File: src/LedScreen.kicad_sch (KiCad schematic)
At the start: 38 parts

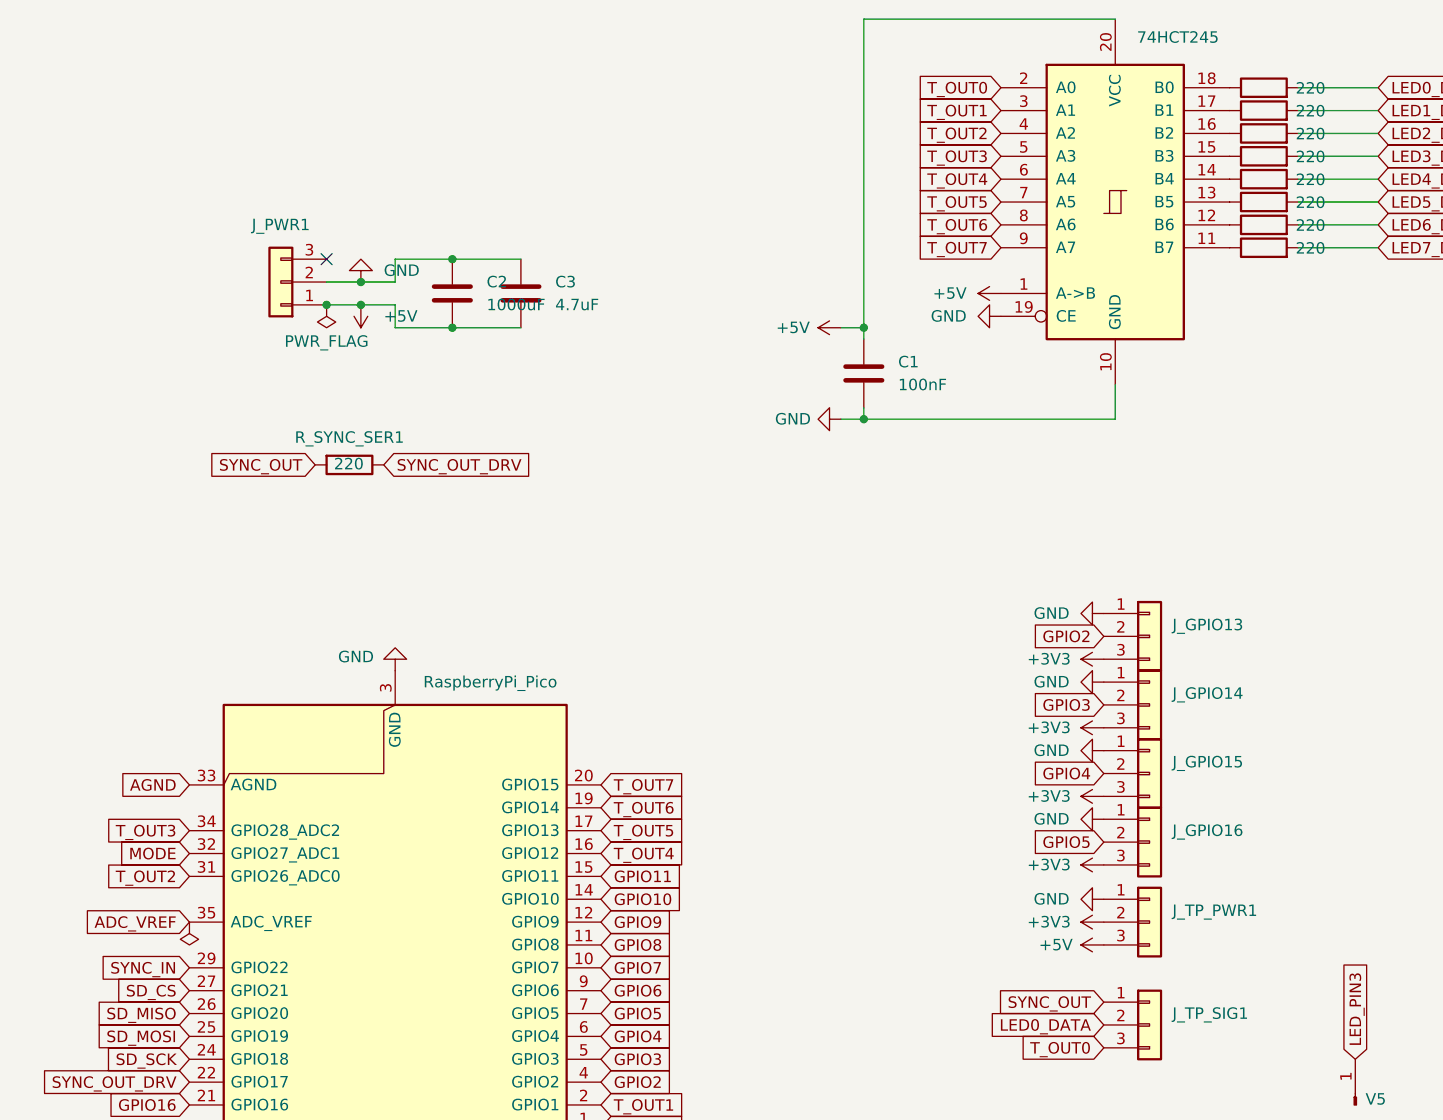
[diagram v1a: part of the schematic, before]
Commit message: added Bom+Journal
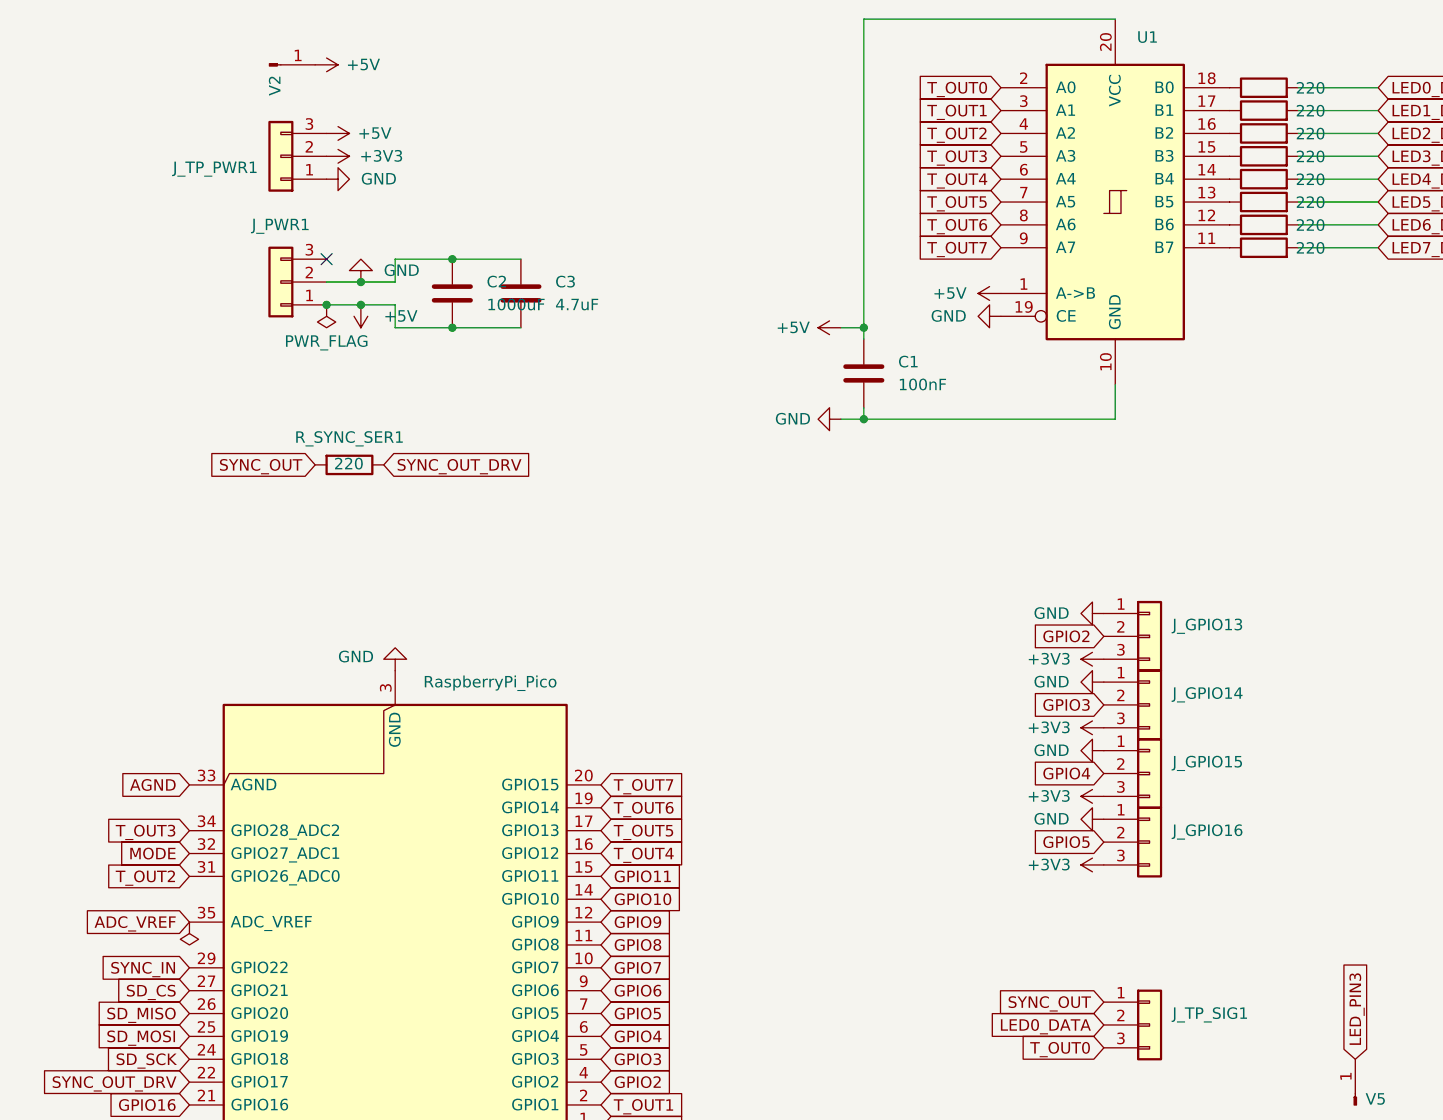
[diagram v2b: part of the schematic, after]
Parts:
- added V2: Conn_01x01_Pin, Connector_PinHeader_2.54mm:PinHeader_1x01_P2.54mm_Vertical, symbol Connector:Conn_01x01_Pin
- renumbered SD_READER1 to J1, 74HCT245 to U1
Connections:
- net +5V: now also V2.1 (Pin_1)
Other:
- moved on the sheet: J_TP_PWR1
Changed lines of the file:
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@@
 	(symbol
 		(lib_id "power:+3V3")
-		(at 132.08 132.08 90)
+		(at 45.72 46.99 270)
 		(unit 1)
 		(exclude_from_sim no)
@@
 		(dnp no)
 		(property "Reference" "#PWR019"
-			(at 135.89 132.08 0)
+			(at 41.91 46.99 0)
 			(effects
 				(font
@@
 		)
 		(property "Value" "+3V3"
-			(at 125.984 132.08 90)
+			(at 51.816 46.99 90)
 			(effects
 				(font
@@
 		)
 		(property "Footprint" ""
-			(at 132.08 132.08 0)
+			(at 45.72 46.99 0)
 			(effects
 				(font
@@
 		)
 		(property "Datasheet" ""
-			(at 132.08 132.08 0)
+			(at 45.72 46.99 0)
 			(effects
 				(font
@@
 		)
 		(property "Description" "Power symbol creates a global label with name \"+3V3\""
-			(at 132.08 132.08 0)
+			(at 45.72 46.99 0)
 			(effects
 				(font
@@
 	)
 	(symbol
+		(lib_id "Connector:Conn_01x01_Pin")
+		(at 39.37 36.83 0)
+		(unit 1)
+		(exclude_from_sim no)
+		(in_bom yes)
+		(on_board yes)
+		(dnp no)
+		(property "Reference" "V2"
+			(at 40.005 39.116 90)
+			(effects
+				(font
+					(size 1.27 1.27)
+				)
+			)
+		)
+		(property "Value" "Conn_01x01_Pin"
+			(at 37.465 37.084 90)
+			(effects
+				(font
+					(size 1.27 1.27)
+				)
+				(hide yes)
+			)
+		)
+		(property "Footprint" "Connector_PinHeader_2.54mm:PinHeader_1x01_P2.54mm_Vertical"
+			(at 38.608 35.052 0)
+			(effects
+				(font
+					(size 1.27 1.27)
+				)
+				(hide yes)
+			)
+		)
+		(property "Datasheet" "~"
+			(at 39.37 36.83 0)
+			(effects
+				(font
+					(size 1.27 1.27)
+				)
+				(hide yes)
+			)
+		)
+		(property "Description" "Generic connector, single row, 01x01, script generated"
+			(at 39.37 36.83 0)
+			(effects
+				(font
+					(size 1.27 1.27)
+				)
+				(hide yes)
+			)
+		)
+		(pin "1"
+		)
+		(instances
+			(project "LedScreen"
+				(path "/6393ae6b-20d3-4709-8a4f-a83a956b3492"
+					(reference "V2")
+					(unit 1)
+				)
+			)
+		)
+	)
+	(symbol
 		(lib_id "Connector_Generic:Conn_01x02")
 		(at 151.13 175.26 0)
@@
 		(on_board yes)
 		(dnp no)
-		(property "Reference" "74HCT245"
+		(property "Reference" "U1"
 			(at 135.7473 33.782 0)
 			(effects
@@
 			(project ""
 				(path "/6393ae6b-20d3-4709-8a4f-a83a956b3492"
-					(reference "74HCT245")
+					(reference "U1")
 					(unit 1)
 				)
@@
 	(symbol
 		(lib_id "power:+5V")
+		(at 44.45 36.83 270)
+		(unit 1)
+		(exclude_from_sim no)
+		(in_bom yes)
+		(on_board yes)
+		(dnp no)
+		(property "Reference" "#PWR046"
+			(at 40.64 36.83 0)
+			(effects
+				(font
+					(size 1.27 1.27)
+				)
+				(hide yes)
+			)
+		)
+		(property "Value" "+5V"
+			(at 49.784 36.83 90)
+			(effects
+				(font
+					(size 1.27 1.27)
+				)
+			)
+		)
+		(property "Footprint" ""
+			(at 44.45 36.83 0)
+			(effects
+				(font
+					(size 1.27 1.27)
+				)
+				(hide yes)
+			)
+		)
+		(property "Datasheet" ""
+			(at 44.45 36.83 0)
+			(effects
+				(font
+					(size 1.27 1.27)
+				)
+				(hide yes)
+			)
+		)
+		(property "Description" "Power symbol creates a global label with name \"+5V\""
+			(at 44.45 36.83 0)
+			(effects
+				(font
+					(size 1.27 1.27)
+				)
+				(hide yes)
+			)
+		)
+		(pin "1"
+		)
+		(instances
+			(project "LedScreen"
+				(path "/6393ae6b-20d3-4709-8a4f-a83a956b3492"
+					(reference "#PWR046")
+					(unit 1)
+				)
+			)
+		)
+	)
+	(symbol
+		(lib_id "power:+5V")
 		(at 182.88 111.76 90)
 		(unit 1)
@@
 	(symbol
 		(lib_id "Connector_Generic:Conn_01x03")
-		(at 137.16 132.08 0)
+		(at 40.64 46.99 180)
 		(unit 1)
 		(exclude_from_sim no)
@@
 		(fields_autoplaced yes)
 		(property "Reference" "J_TP_PWR1"
-			(at 139.7 130.8099 0)
+			(at 38.1 48.2601 0)
 			(effects
 				(font
@@
 		)
 		(property "Value" "TP_PWR"
-			(at 139.7 133.3499 0)
+			(at 38.1 45.7201 0)
 			(effects
 				(font
@@
 		)
 		(property "Footprint" "Connector_PinHeader_2.54mm:PinHeader_1x03_P2.54mm_Vertical"
-			(at 137.16 132.08 0)
+			(at 40.64 46.99 0)
 			(effects
 				(font
@@
 		)
 		(property "Datasheet" "~"
-			(at 137.16 132.08 0)
+			(at 40.64 46.99 0)
 			(effects
 				(font
@@
 		)
 		(property "Description" "Generic connector, single row, 01x03, script generated (kicad-library-utils/schlib/autogen/connector/)"
-			(at 137.16 132.08 0)
+			(at 40.64 46.99 0)
 			(effects
 				(font
@@
 	(symbol
 		(lib_id "power:+5V")
-		(at 132.08 134.62 90)
+		(at 45.72 44.45 270)
 		(unit 1)
 		(exclude_from_sim no)
@@
 		(dnp no)
 		(property "Reference" "#PWR030"
-			(at 135.89 134.62 0)
+			(at 41.91 44.45 0)
 			(effects
 				(font
@@
 		)
 		(property "Value" "+5V"
-			(at 126.746 134.62 90)
+			(at 51.054 44.45 90)
 			(effects
 				(font
@@
 		)
 		(property "Footprint" ""
-			(at 132.08 134.62 0)
+			(at 45.72 44.45 0)
 			(effects
 				(font
@@
 		)
 		(property "Datasheet" ""
-			(at 132.08 134.62 0)
+			(at 45.72 44.45 0)
 			(effects
 				(font
@@
 		)
 		(property "Description" "Power symbol creates a global label with name \"+5V\""
-			(at 132.08 134.62 0)
+			(at 45.72 44.45 0)
 			(effects
 				(font
@@
 	(symbol
 		(lib_id "power:GND")
-		(at 132.08 129.54 270)
+		(at 45.72 49.53 90)
 		(unit 1)
 		(exclude_from_sim no)
@@
 		(fields_autoplaced yes)
 		(property "Reference" "#PWR032"
-			(at 125.73 129.54 0)
+			(at 52.07 49.53 0)
 			(effects
 				(font
@@
 		)
 		(property "Value" "GND"
-			(at 128.27 129.5399 90)
+			(at 49.53 49.5301 90)
 			(effects
 				(font
@@
 		)
 		(property "Footprint" ""
-			(at 132.08 129.54 0)
+			(at 45.72 49.53 0)
 			(effects
 				(font
@@
 		)
 		(property "Datasheet" ""
-			(at 132.08 129.54 0)
+			(at 45.72 49.53 0)
 			(effects
 				(font
@@
 		)
 		(property "Description" "Power symbol creates a global label with name \"GND\" , ground"
-			(at 132.08 129.54 0)
+			(at 45.72 49.53 0)
 			(effects
 				(font
@@
 		(on_board yes)
 		(dnp no)
-		(property "Reference" "SD_READER1"
+		(property "Reference" "J1"
 			(at 242.951 28.194 0)
 			(effects
@@
 			(project ""
 				(path "/6393ae6b-20d3-4709-8a4f-a83a956b3492"
-					(reference "SD_READER1")
+					(reference "J1")
 					(unit 1)
 				)

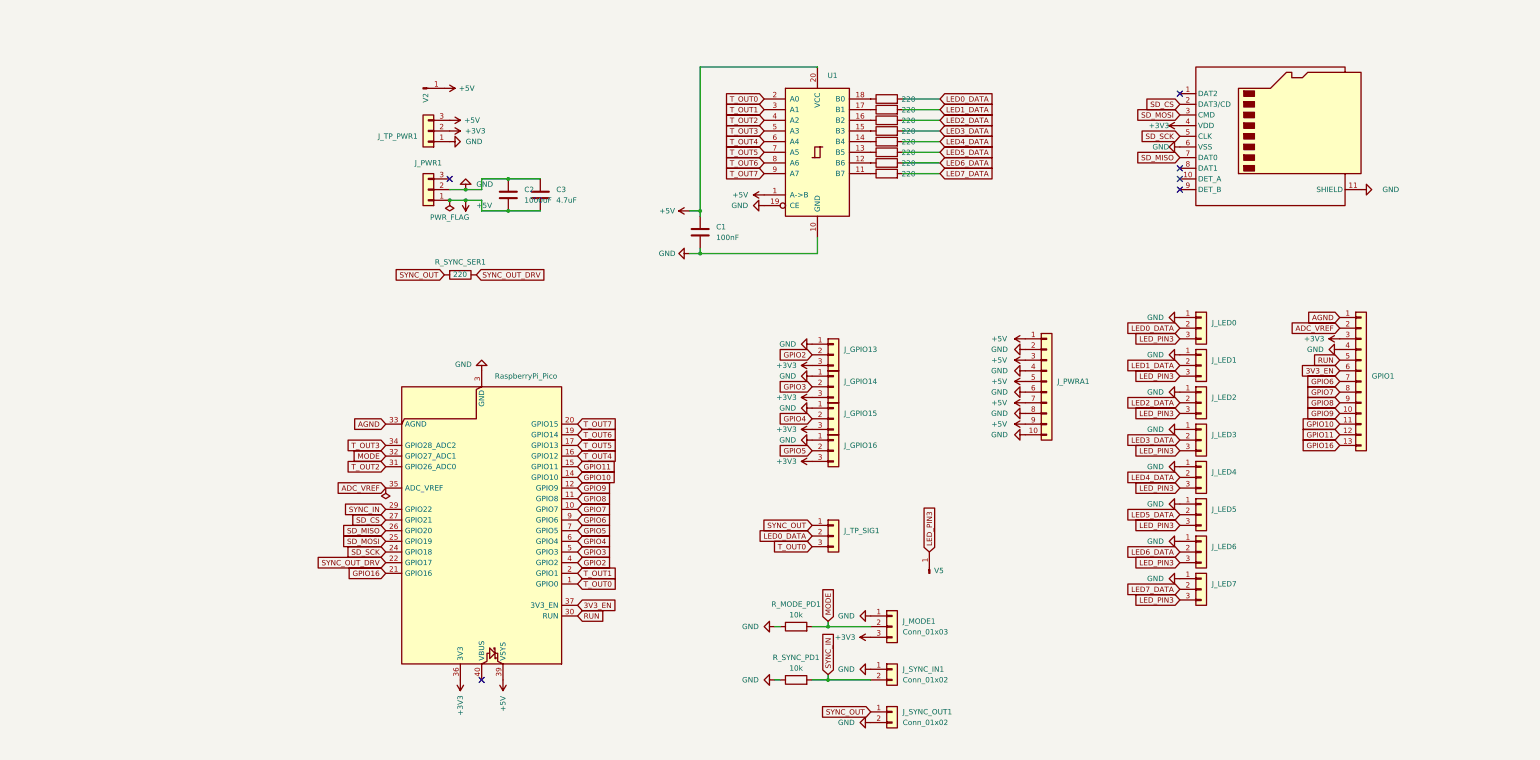
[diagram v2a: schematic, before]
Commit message: updated power injection wireing
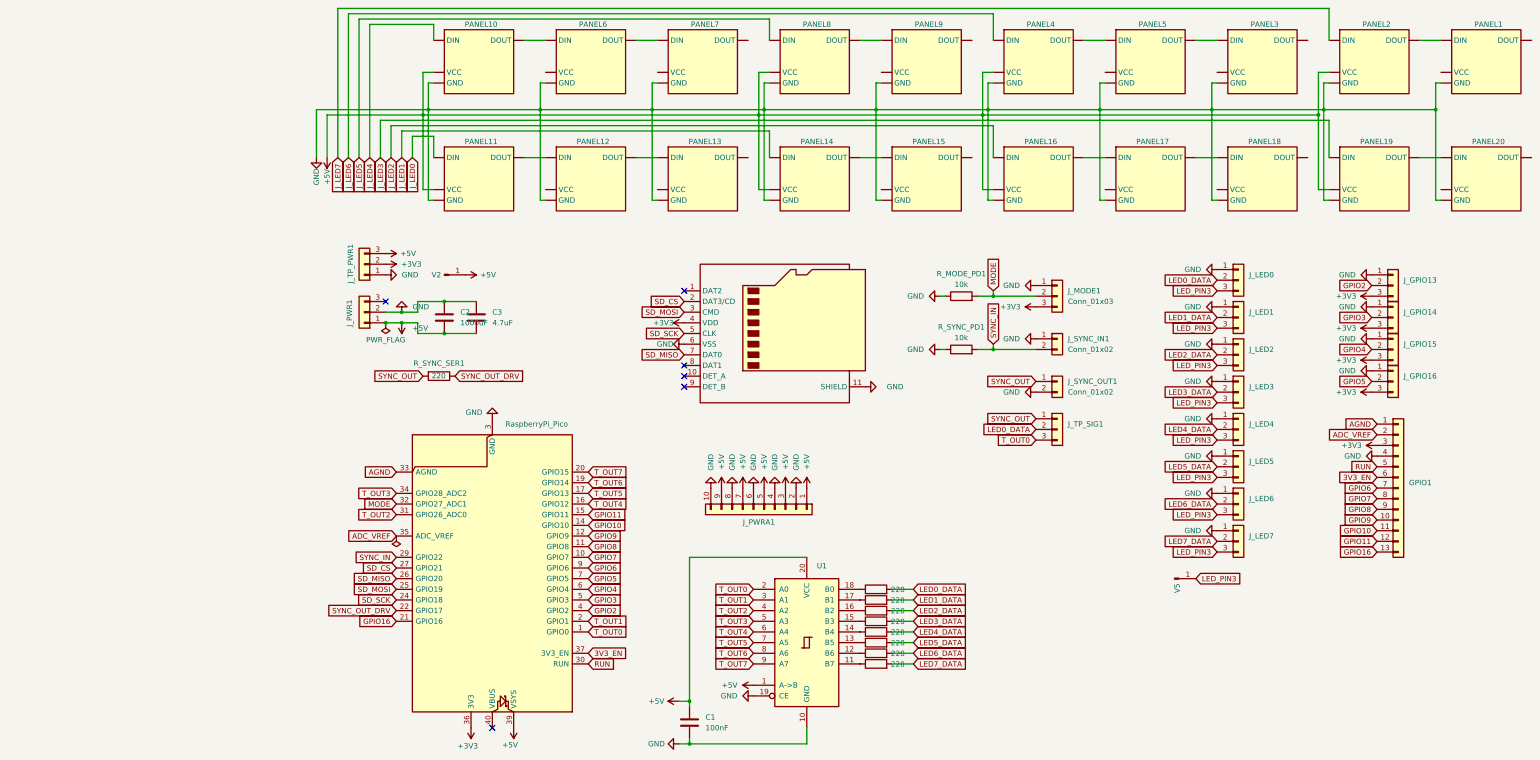
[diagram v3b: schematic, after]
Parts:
- added PANEL1, PANEL10, PANEL11, PANEL12, PANEL13, PANEL14, PANEL15, PANEL16, PANEL17, PANEL18, PANEL19, PANEL2, PANEL20, PANEL3, PANEL4, PANEL5, PANEL6, PANEL7, PANEL8, PANEL9: ~, symbol ledpanels:LED_PANEL_16x16
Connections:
- net +5V: now also PANEL10. (DOUT), PANEL11. (DOUT), PANEL14. (DOUT), PANEL16. (DOUT), PANEL19. (DOUT), PANEL2. (DOUT), PANEL4. (DOUT), PANEL8. (DOUT)
- net GND: now also PANEL1. (DOUT), PANEL10. (DOUT), PANEL11. (DOUT), PANEL12. (DOUT), PANEL13. (DOUT), PANEL14. (DOUT), PANEL15. (DOUT), PANEL16. (DOUT), PANEL17. (DOUT), PANEL18. (DOUT), PANEL19. (DOUT), PANEL2. (DOUT), PANEL20. (DOUT), PANEL3. (DOUT), PANEL4. (DOUT), PANEL5. (DOUT), PANEL6. (DOUT), PANEL7. (DOUT), PANEL8. (DOUT), PANEL9. (DOUT)
- new net: PANEL8. (DOUT), PANEL9. (DOUT)
- new net: PANEL4. (DOUT), PANEL5. (DOUT)
- new net: PANEL1. (DOUT), PANEL2. (DOUT)
- new net: PANEL19. (DOUT), PANEL20. (DOUT)
- new net: PANEL6. (DOUT), PANEL7. (DOUT)
- new net: PANEL16. (DOUT), PANEL17. (DOUT)
- new net: PANEL12. (DOUT), PANEL13. (DOUT)
- new net: PANEL3. (DOUT), PANEL5. (DOUT)
- new net: PANEL10. (DOUT), PANEL6. (DOUT)
- new net: PANEL17. (DOUT), PANEL18. (DOUT)
- new net: PANEL14. (DOUT), PANEL15. (DOUT)
- new net: PANEL11. (DOUT), PANEL12. (DOUT)
- new net J_LED0: PANEL11. (DOUT)
- new net J_LED1: PANEL14. (DOUT)
- new net J_LED2: PANEL16. (DOUT)
- new net J_LED3: PANEL19. (DOUT)
- new net J_LED4: PANEL10. (DOUT)
- new net J_LED5: PANEL8. (DOUT)
- new net J_LED6: PANEL4. (DOUT)
- new net J_LED7: PANEL2. (DOUT)
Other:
- moved on the sheet: C1, C2, C3, GPIO1, J_GPIO13, J_GPIO14, J_GPIO15, J_GPIO16, J_LED0, J_LED1, J_LED2, J_LED3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
